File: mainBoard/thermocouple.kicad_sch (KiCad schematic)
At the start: 57 parts, among them J4 4DB-P108-02, J5 4DB-P108-02, J6 4DB-P108-02, U10 DS18B20+, U11 DS18B20+, U12 OPA333AIDCKT, U13 DS18B20+, U8 OPA333AIDCKT, U9 OPA333AIDCKT

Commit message: board routing nearly complete
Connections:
- net TC2_ADC: now also C38.1, R46.2; no longer C34.1, R39.2
- net TC2_ADC_RC: now also R46.1; no longer R39.1
- net TC2_N: now also J5.1 (Pin_1); no longer J5.2 (Pin_2)
- net TC2_P: now also J5.2 (Pin_2); no longer J5.1 (Pin_1)
- net TC3_ADC: now also C34.1, R39.2; no longer C38.1, R46.2
- net TC3_ADC_RC: now also R39.1; no longer R46.1
- net TC3_N: now also J6.1 (Pin_1); no longer J6.2 (Pin_2)
- net TC3_P: now also J6.2 (Pin_2); no longer J6.1 (Pin_1)
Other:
- moved on the sheet: C34, C38, J5, J6, R39, R46
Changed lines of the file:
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@@
 	(symbol
 		(lib_id "Device:R_US")
-		(at 177.8 203.2 90)
+		(at 365.76 93.98 90)
 		(unit 1)
 		(body_style 1)
@@
 		(fields_autoplaced yes)
 		(property "Reference" "R39"
-			(at 177.8 196.85 90)
+			(at 365.76 87.63 90)
 			(show_name no)
 			(do_not_autoplace no)
@@
 		)
 		(property "Value" "1k"
-			(at 177.8 199.39 90)
+			(at 365.76 90.17 90)
 			(show_name no)
 			(do_not_autoplace no)
@@
 		)
 		(property "Footprint" "Resistor_SMD:R_0603_1608Metric_Pad0.98x0.95mm_HandSolder"
-			(at 178.054 202.184 90)
-			(hide yes)
-			(show_name no)
-			(do_not_autoplace no)
-			(effects
-				(font
-					(size 1.27 1.27)
-				)
-			)
-		)
-		(property "Datasheet" ""
-			(at 177.8 203.2 0)
+			(at 366.014 92.964 90)
+			(hide yes)
+			(show_name no)
+			(do_not_autoplace no)
+			(effects
+				(font
+					(size 1.27 1.27)
+				)
+			)
+		)
+		(property "Datasheet" ""
+			(at 365.76 93.98 0)
 			(hide yes)
 			(show_name no)
@@
 		)
 		(property "Description" "Resistor, US symbol"
-			(at 177.8 203.2 0)
+			(at 365.76 93.98 0)
 			(hide yes)
 			(show_name no)
@@
 	(symbol
 		(lib_id "Connector_Generic:Conn_01x02")
-		(at 43.18 227.33 0)
-		(mirror y)
+		(at 43.18 229.87 180)
 		(unit 1)
 		(body_style 1)
@@
 		(dnp no)
 		(property "Reference" "J5"
-			(at 43.18 221.742 0)
+			(at 43.18 235.458 0)
 			(show_name no)
 			(do_not_autoplace no)
@@
 		)
 		(property "Value" "4DB-P108-02"
-			(at 43.18 224.028 0)
+			(at 43.18 233.172 0)
 			(show_name no)
 			(do_not_autoplace no)
@@
 		)
 		(property "Footprint" "4DB_P108_02:CONN_4DB-P108-02_TEC"
-			(at 43.18 227.33 0)
-			(hide yes)
-			(show_name no)
-			(do_not_autoplace no)
-			(effects
-				(font
-					(size 1.27 1.27)
-				)
-			)
-		)
-		(property "Datasheet" ""
-			(at 43.18 227.33 0)
+			(at 43.18 229.87 0)
+			(hide yes)
+			(show_name no)
+			(do_not_autoplace no)
+			(effects
+				(font
+					(size 1.27 1.27)
+				)
+			)
+		)
+		(property "Datasheet" ""
+			(at 43.18 229.87 0)
 			(hide yes)
 			(show_name no)
@@
 		)
 		(property "Description" "Generic connector, single row, 01x02, script generated (kicad-library-utils/schlib/autogen/connector/)"
-			(at 43.18 227.33 0)
+			(at 43.18 229.87 0)
 			(hide yes)
 			(show_name no)
@@
 	(symbol
 		(lib_id "Device:R_US")
-		(at 365.76 93.98 90)
+		(at 177.8 203.2 90)
 		(unit 1)
 		(body_style 1)
@@
 		(fields_autoplaced yes)
 		(property "Reference" "R46"
-			(at 365.76 87.63 90)
+			(at 177.8 196.85 90)
 			(show_name no)
 			(do_not_autoplace no)
@@
 		)
 		(property "Value" "1k"
-			(at 365.76 90.17 90)
+			(at 177.8 199.39 90)
 			(show_name no)
 			(do_not_autoplace no)
@@
 		)
 		(property "Footprint" "Resistor_SMD:R_0603_1608Metric_Pad0.98x0.95mm_HandSolder"
-			(at 366.014 92.964 90)
-			(hide yes)
-			(show_name no)
-			(do_not_autoplace no)
-			(effects
-				(font
-					(size 1.27 1.27)
-				)
-			)
-		)
-		(property "Datasheet" ""
-			(at 365.76 93.98 0)
+			(at 178.054 202.184 90)
+			(hide yes)
+			(show_name no)
+			(do_not_autoplace no)
+			(effects
+				(font
+					(size 1.27 1.27)
+				)
+			)
+		)
+		(property "Datasheet" ""
+			(at 177.8 203.2 0)
 			(hide yes)
 			(show_name no)
@@
 		)
 		(property "Description" "Resistor, US symbol"
-			(at 365.76 93.98 0)
+			(at 177.8 203.2 0)
 			(hide yes)
 			(show_name no)
@@
 	(symbol
 		(lib_id "Device:C")
-		(at 370.84 101.6 0)
+		(at 182.88 210.82 0)
 		(unit 1)
 		(body_style 1)
@@
 		(fields_autoplaced yes)
 		(property "Reference" "C38"
-			(at 374.65 100.3299 0)
+			(at 186.69 209.5499 0)
 			(show_name no)
 			(do_not_autoplace no)
@@
 		)
 		(property "Value" "10uF"
-			(at 374.65 102.8699 0)
+			(at 186.69 212.0899 0)
 			(show_name no)
 			(do_not_autoplace no)
@@
 		)
 		(property "Footprint" "Capacitor_SMD:C_0603_1608Metric_Pad1.08x0.95mm_HandSolder"
-			(at 371.8052 105.41 0)
-			(hide yes)
-			(show_name no)
-			(do_not_autoplace no)
-			(effects
-				(font
-					(size 1.27 1.27)
-				)
-			)
-		)
-		(property "Datasheet" ""
-			(at 370.84 101.6 0)
+			(at 183.8452 214.63 0)
+			(hide yes)
+			(show_name no)
+			(do_not_autoplace no)
+			(effects
+				(font
+					(size 1.27 1.27)
+				)
+			)
+		)
+		(property "Datasheet" ""
+			(at 182.88 210.82 0)
 			(hide yes)
 			(show_name no)
@@
 		)
 		(property "Description" "Unpolarized capacitor"
-			(at 370.84 101.6 0)
+			(at 182.88 210.82 0)
 			(hide yes)
 			(show_name no)
@@
 	(symbol
 		(lib_id "Device:C")
-		(at 182.88 210.82 0)
+		(at 370.84 101.6 0)
 		(unit 1)
 		(body_style 1)
@@
 		(fields_autoplaced yes)
 		(property "Reference" "C34"
-			(at 186.69 209.5499 0)
+			(at 374.65 100.3299 0)
 			(show_name no)
 			(do_not_autoplace no)
@@
 		)
 		(property "Value" "10uF"
-			(at 186.69 212.0899 0)
+			(at 374.65 102.8699 0)
 			(show_name no)
 			(do_not_autoplace no)
@@
 		)
 		(property "Footprint" "Capacitor_SMD:C_0603_1608Metric_Pad1.08x0.95mm_HandSolder"
-			(at 183.8452 214.63 0)
-			(hide yes)
-			(show_name no)
-			(do_not_autoplace no)
-			(effects
-				(font
-					(size 1.27 1.27)
-				)
-			)
-		)
-		(property "Datasheet" ""
-			(at 182.88 210.82 0)
+			(at 371.8052 105.41 0)
+			(hide yes)
+			(show_name no)
+			(do_not_autoplace no)
+			(effects
+				(font
+					(size 1.27 1.27)
+				)
+			)
+		)
+		(property "Datasheet" ""
+			(at 370.84 101.6 0)
 			(hide yes)
 			(show_name no)
@@
 		)
 		(property "Description" "Unpolarized capacitor"
-			(at 182.88 210.82 0)
+			(at 370.84 101.6 0)
 			(hide yes)
 			(show_name no)
@@
 	(symbol
 		(lib_id "Connector_Generic:Conn_01x02")
-		(at 231.14 118.11 0)
-		(mirror y)
+		(at 231.14 120.65 180)
 		(unit 1)
 		(body_style 1)
@@
 		(dnp no)
 		(property "Reference" "J6"
-			(at 231.14 112.522 0)
+			(at 231.14 126.238 0)
 			(show_name no)
 			(do_not_autoplace no)
@@
 		)
 		(property "Value" "4DB-P108-02"
-			(at 231.14 114.808 0)
+			(at 231.14 123.952 0)
 			(show_name no)
 			(do_not_autoplace no)
@@
 		)
 		(property "Footprint" "4DB_P108_02:CONN_4DB-P108-02_TEC"
-			(at 231.14 118.11 0)
-			(hide yes)
-			(show_name no)
-			(do_not_autoplace no)
-			(effects
-				(font
-					(size 1.27 1.27)
-				)
-			)
-		)
-		(property "Datasheet" ""
-			(at 231.14 118.11 0)
+			(at 231.14 120.65 0)
+			(hide yes)
+			(show_name no)
+			(do_not_autoplace no)
+			(effects
+				(font
+					(size 1.27 1.27)
+				)
+			)
+		)
+		(property "Datasheet" ""
+			(at 231.14 120.65 0)
 			(hide yes)
 			(show_name no)
@@
 		)
 		(property "Description" "Generic connector, single row, 01x02, script generated (kicad-library-utils/schlib/autogen/connector/)"
-			(at 231.14 118.11 0)
-			(hide yes)
-			(show_name no)
+			(at 231.14 120.65 0)
+			(hide yes)
+			(show_name no)

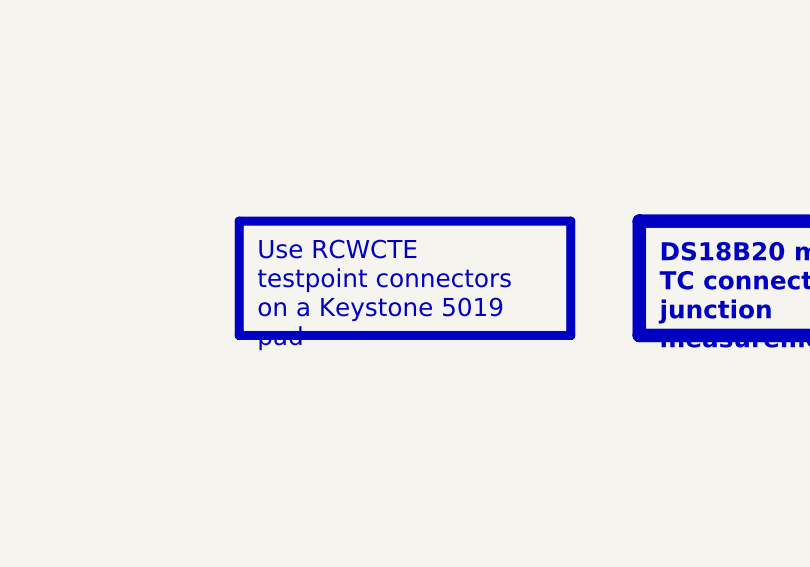
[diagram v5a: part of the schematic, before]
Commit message: 3d models added to PCB
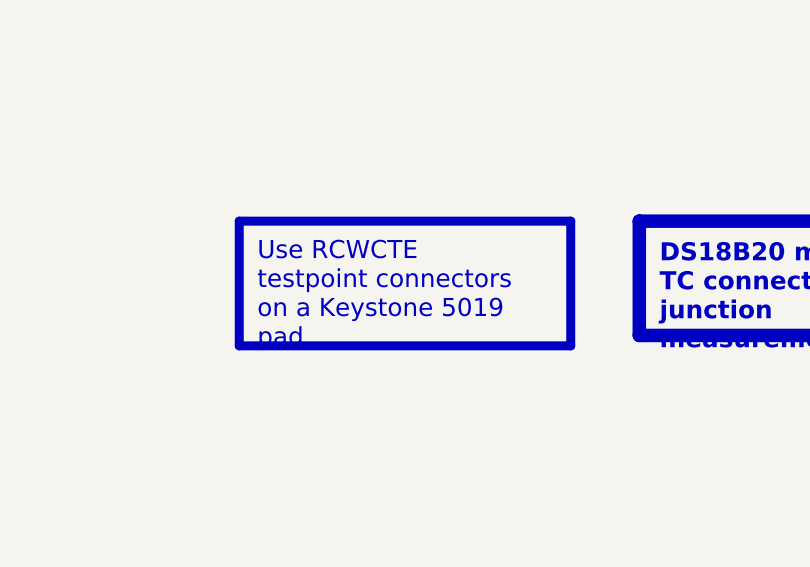
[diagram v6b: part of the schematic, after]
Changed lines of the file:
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@@
 		(exclude_from_sim no)
 		(at 238.76 196.85 0)
-		(size 36.83 12.7)
+		(size 36.83 13.854)
 		(margins 2 2 2 2)
 		(stroke

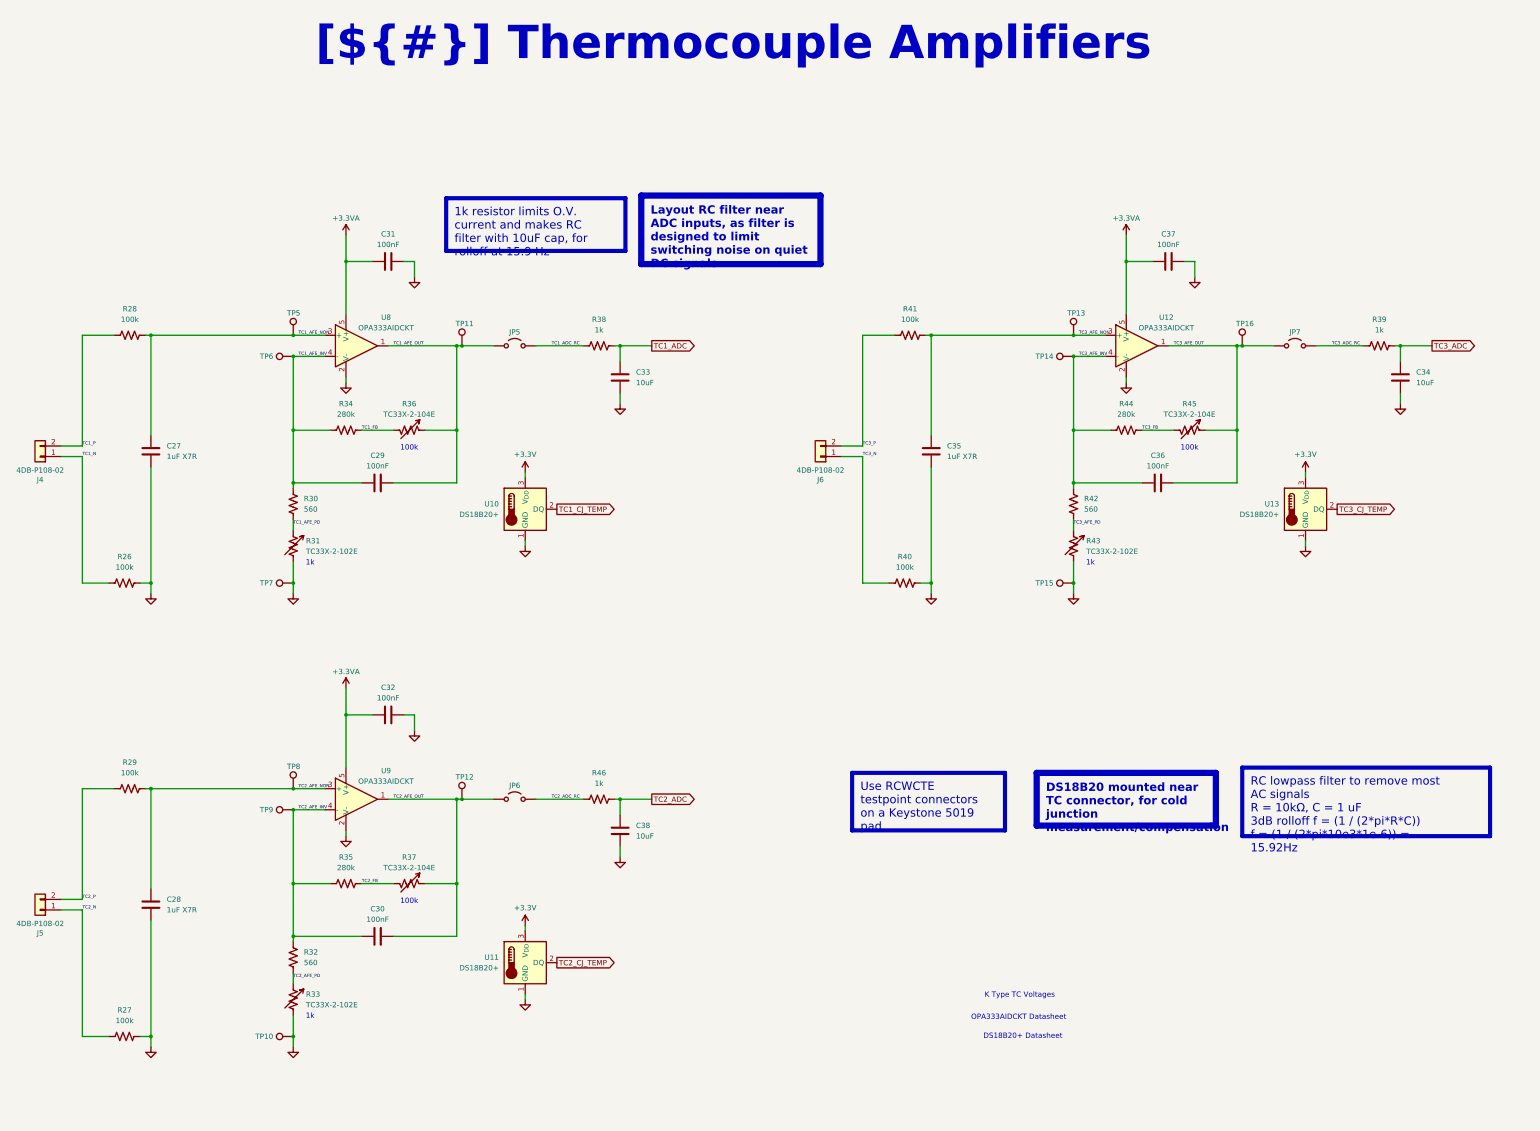
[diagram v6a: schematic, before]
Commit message: change to C0G caps for thermocouple amps
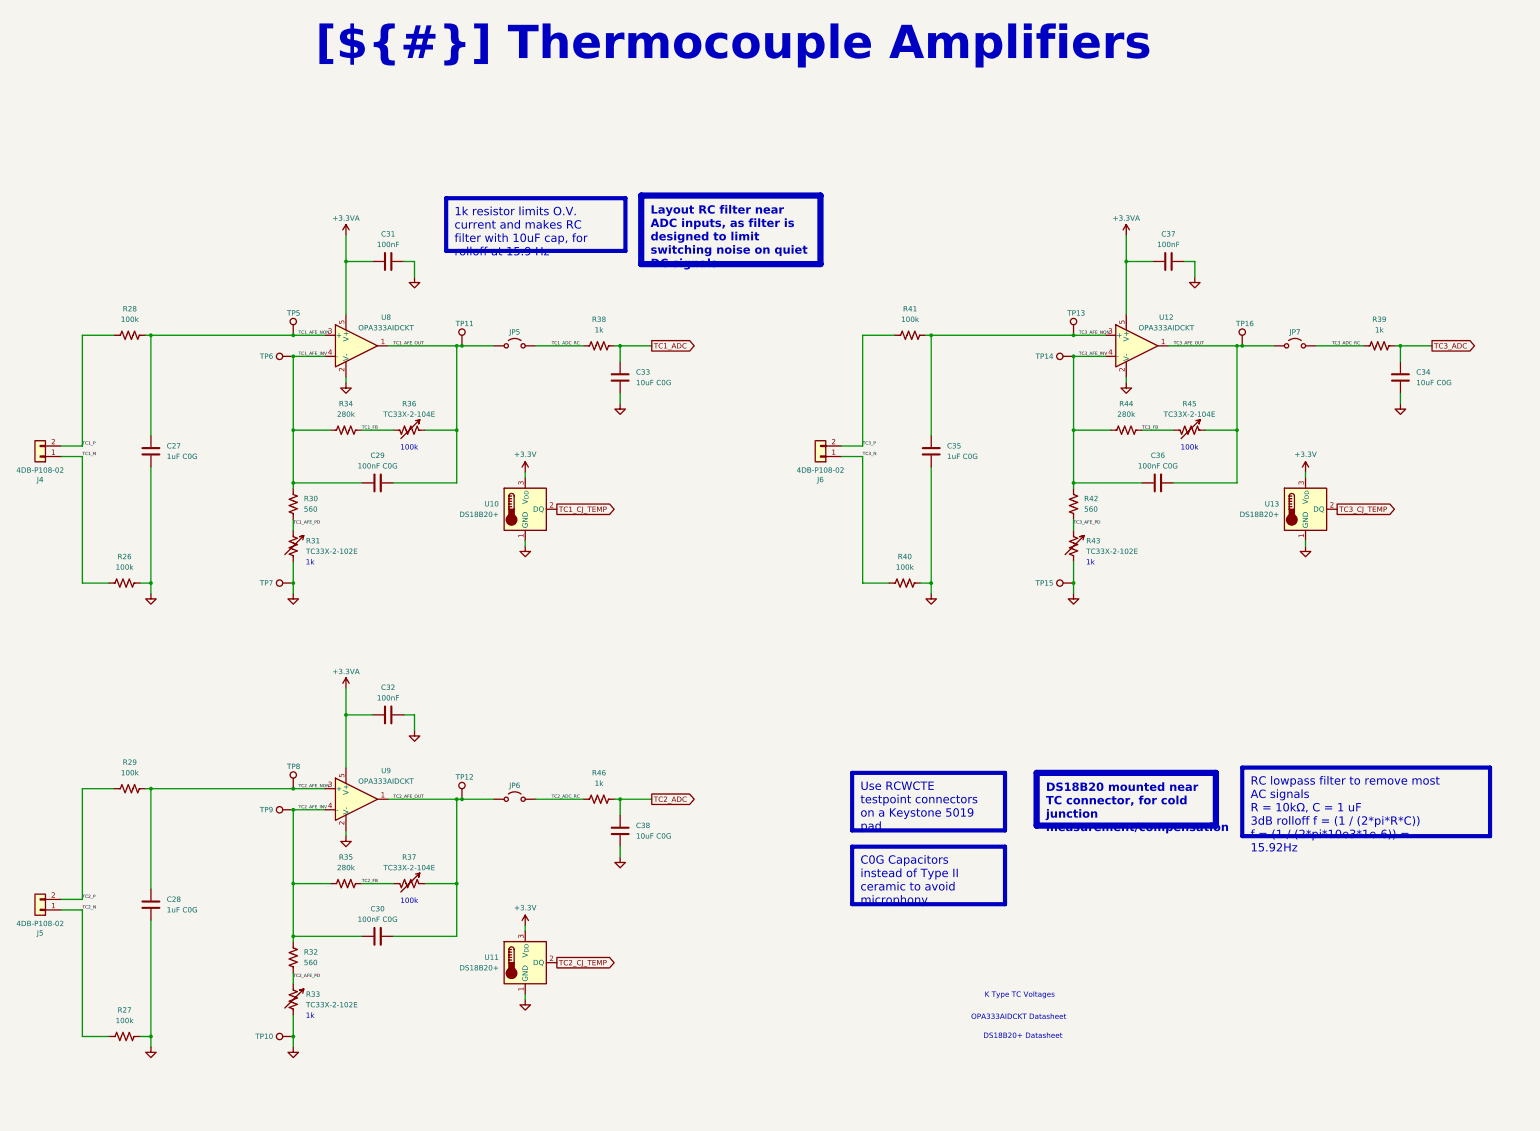
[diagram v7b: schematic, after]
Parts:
- C27, C28, C35: value 1uF X7R -> 1uF C0G
- C29, C30, C36: value 100nF -> 100nF C0G
- C33, C34, C38: value 10uF -> 10uF C0G
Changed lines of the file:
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@@
 		)
 	)
+	(text_box "C0G Capacitors instead of Type II ceramic to avoid microphony"
+		(exclude_from_sim no)
+		(at 238.76 214.63 0)
+		(size 36.83 13.854)
+		(margins 2 2 2 2)
+		(stroke
+			(width 1)
+			(type solid)
+			(color 200 200 200 1)
+		)
+		(fill
+			(type none)
+		)
+		(effects
+			(font
+				(face "Arial")
+				(size 2 2)
+				(color 0 0 0 1)
+			)
+			(justify left top)
+		)
+	)
 	(junction
 		(at 69.85 260.35)
@@
 			)
 		)
-		(property "Value" "1uF X7R"
+		(property "Value" "1uF C0G"
 			(at 73.66 229.8699 0)
 			(show_name no)
@@
 			)
 		)
-		(property "Value" "100nF"
+		(property "Value" "100nF C0G"
 			(at 124.46 232.156 90)
 			(show_name no)
@@
 			)
 		)
-		(property "Value" "100nF"
+		(property "Value" "100nF C0G"
 			(at 124.46 122.936 90)
 			(show_name no)
@@
 			)
 		)
-		(property "Value" "1uF X7R"
+		(property "Value" "1uF C0G"
 			(at 261.62 120.6499 0)
 			(show_name no)
@@
 			)
 		)
-		(property "Value" "10uF"
+		(property "Value" "10uF C0G"
 			(at 186.69 212.0899 0)
 			(show_name no)
@@
 			)
 		)
-		(property "Value" "10uF"
+		(property "Value" "10uF C0G"
 			(at 374.65 102.8699 0)
 			(show_name no)
@@
 			)
 		)
-		(property "Value" "100nF"
+		(property "Value" "100nF C0G"
 			(at 312.42 122.936 90)
 			(show_name no)
@@
 			)
 		)
-		(property "Value" "10uF"
+		(property "Value" "10uF C0G"
 			(at 186.69 102.8699 0)
 			(show_name no)
@@
 			)
 		)
-		(property "Value" "1uF X7R"
+		(property "Value" "1uF C0G"
 			(at 73.66 120.6499 0)
 			(show_name no)
